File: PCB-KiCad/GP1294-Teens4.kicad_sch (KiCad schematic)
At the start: 13 parts, among them U8 CS8421

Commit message: Fixed merge issues.
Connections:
- net DATA_OUT: now also U8.5 (DATA_OUT)
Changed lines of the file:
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@@
+    (stroke (width 0) (type default))
+  )
+  (wire (pts (xy 129.54 51.308) (xy 113.284 51.308))
     (stroke (width 0) (type default))
   )

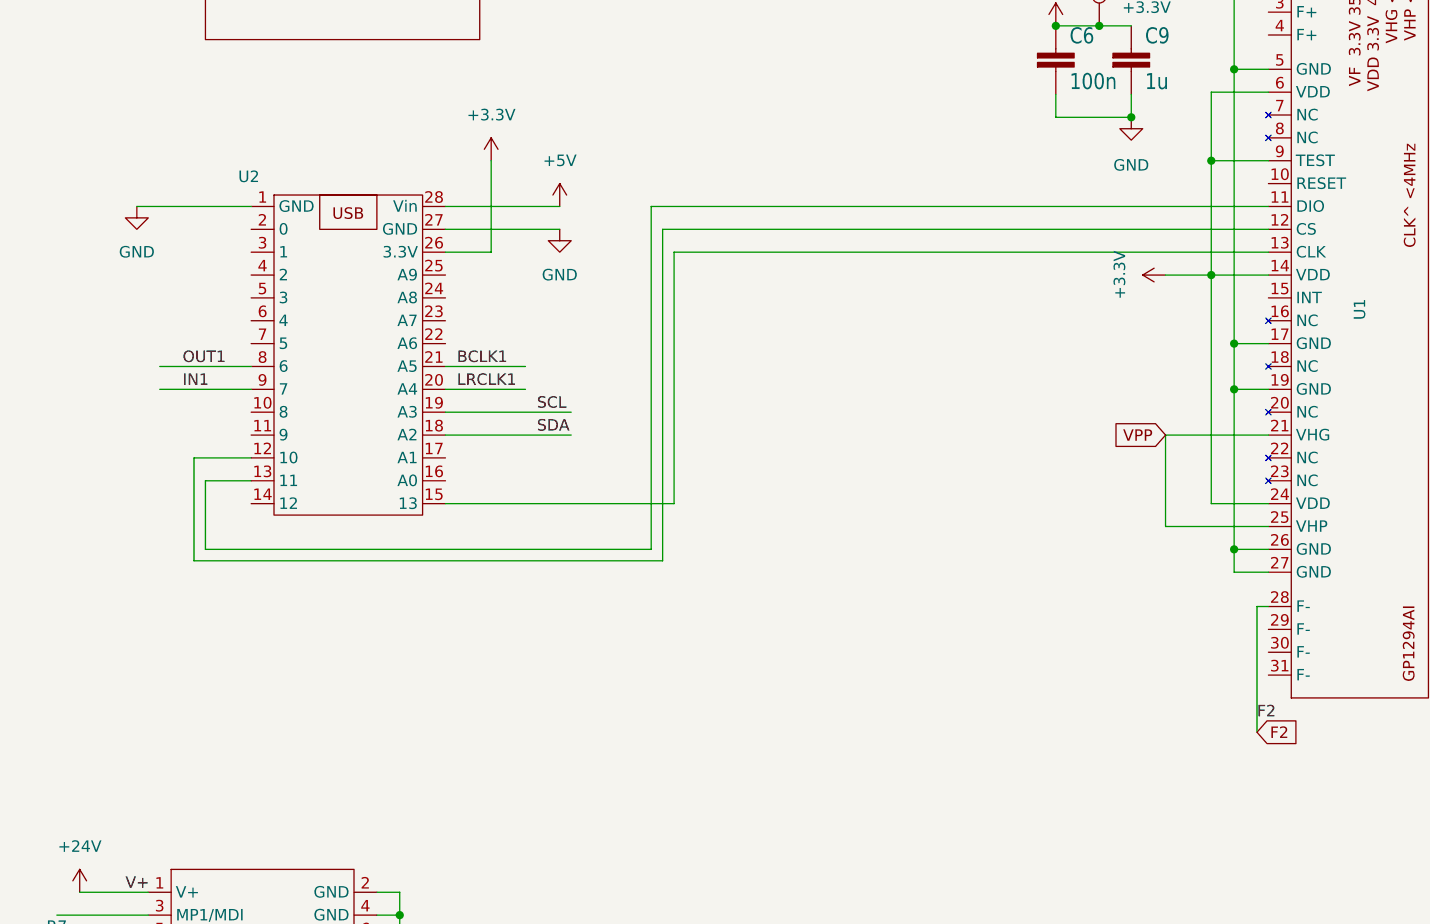
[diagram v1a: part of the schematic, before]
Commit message: Added OLED 5.5" option
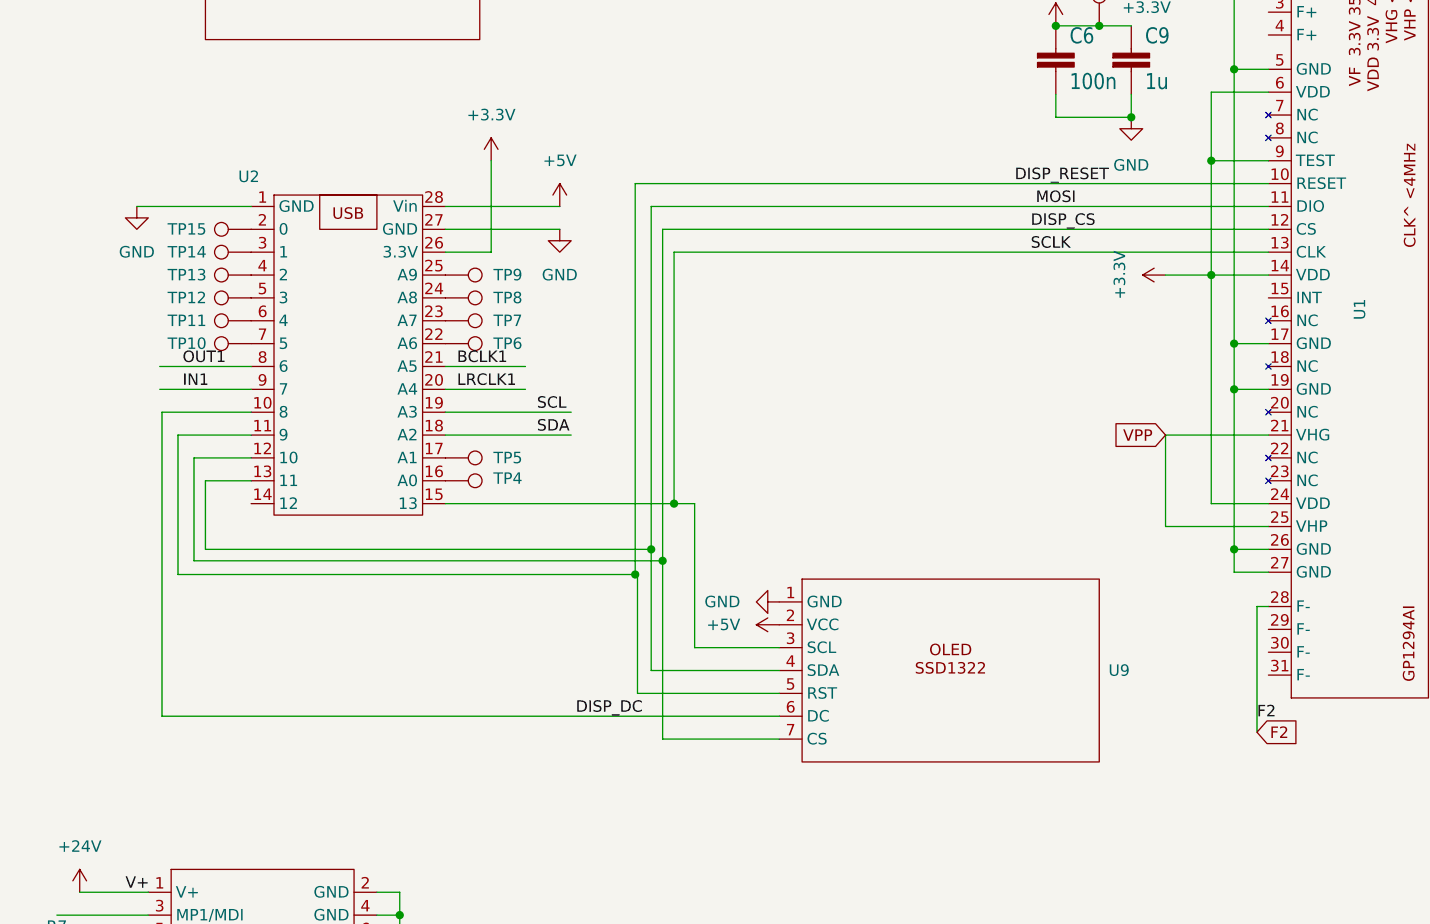
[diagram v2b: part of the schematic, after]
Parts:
- added TP10, TP11, TP12, TP13, TP14, TP15, TP4, TP5, TP6, TP7, TP8, TP9: TestPoint, TestPoint:TestPoint_Pad_2.0x2.0mm, symbol Connector:TestPoint
- added U9: ~, VFDs-Library:OLED5.5, symbol VFDs-Library:OLED5.5
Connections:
- net +5V: now also U9.2 (VCC)
- net GND: now also U9.1 (GND)
- net DISP_RESET: now reaches U1.10 (RESET)
- net DISP_RESET: now also U2.11 (9), U9.5 (RST)
- net MOSI: now reaches U1.11 (DIO), U2.13 (11)
- net MOSI: now also U9.4 (SDA)
- net DISP_CS: now reaches U1.12 (CS), U2.12 (10)
- net DISP_CS: now also U9.7 (CS)
- net SCLK: now reaches U1.13 (CLK), U2.15 (13)
- net SCLK: now also U9.3 (SCL)
- net DISP_DC: now reaches U2.10 (8)
- net DISP_DC: now also U9.6 (DC)
- net at U2.16 (A0): now also TP4.1
- net at U2.17 (A1): now also TP5.1
- net at U2.2 (0): now also TP15.1
- net at U2.22 (A6): now also TP6.1
- net at U2.23 (A7): now also TP7.1
- net at U2.24 (A8): now also TP8.1
- net at U2.25 (A9): now also TP9.1
- net at U2.3 (1): now also TP14.1
- net at U2.4 (2): now also TP13.1
- net at U2.5 (3): now also TP12.1
- net at U2.6 (4): now also TP11.1
- net at U2.7 (5): now also TP10.1

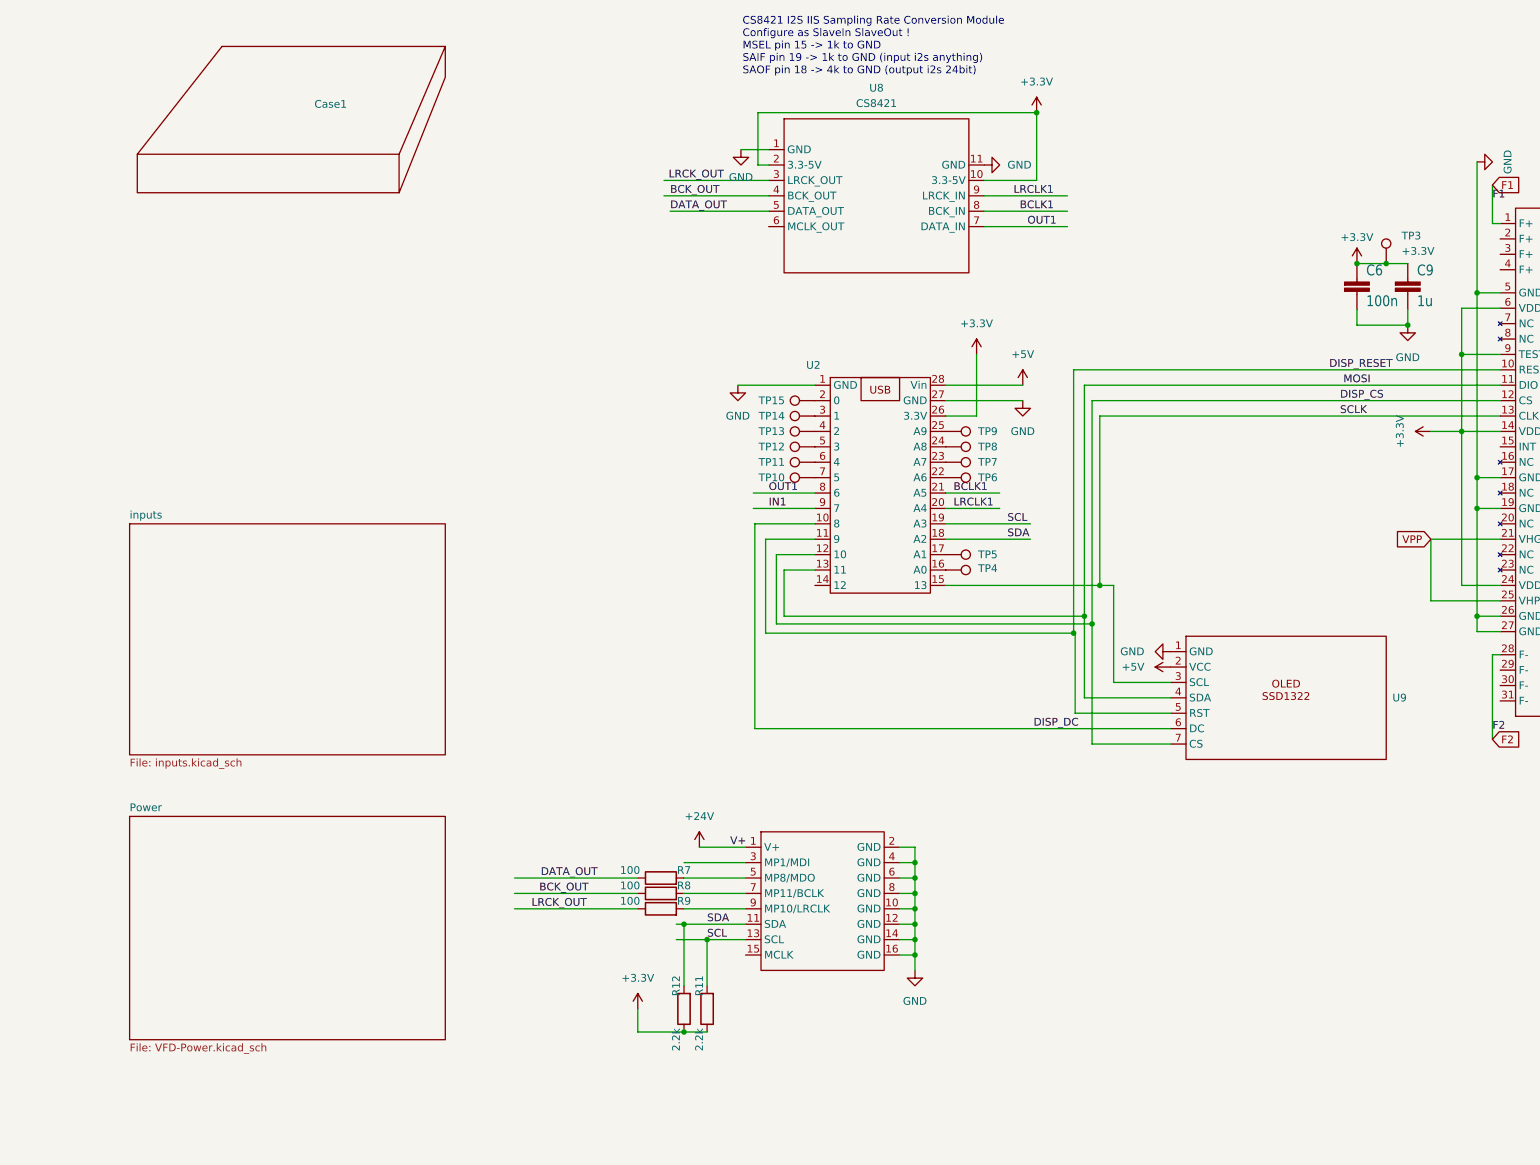
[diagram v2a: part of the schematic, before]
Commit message: Upgraded Power circuit.
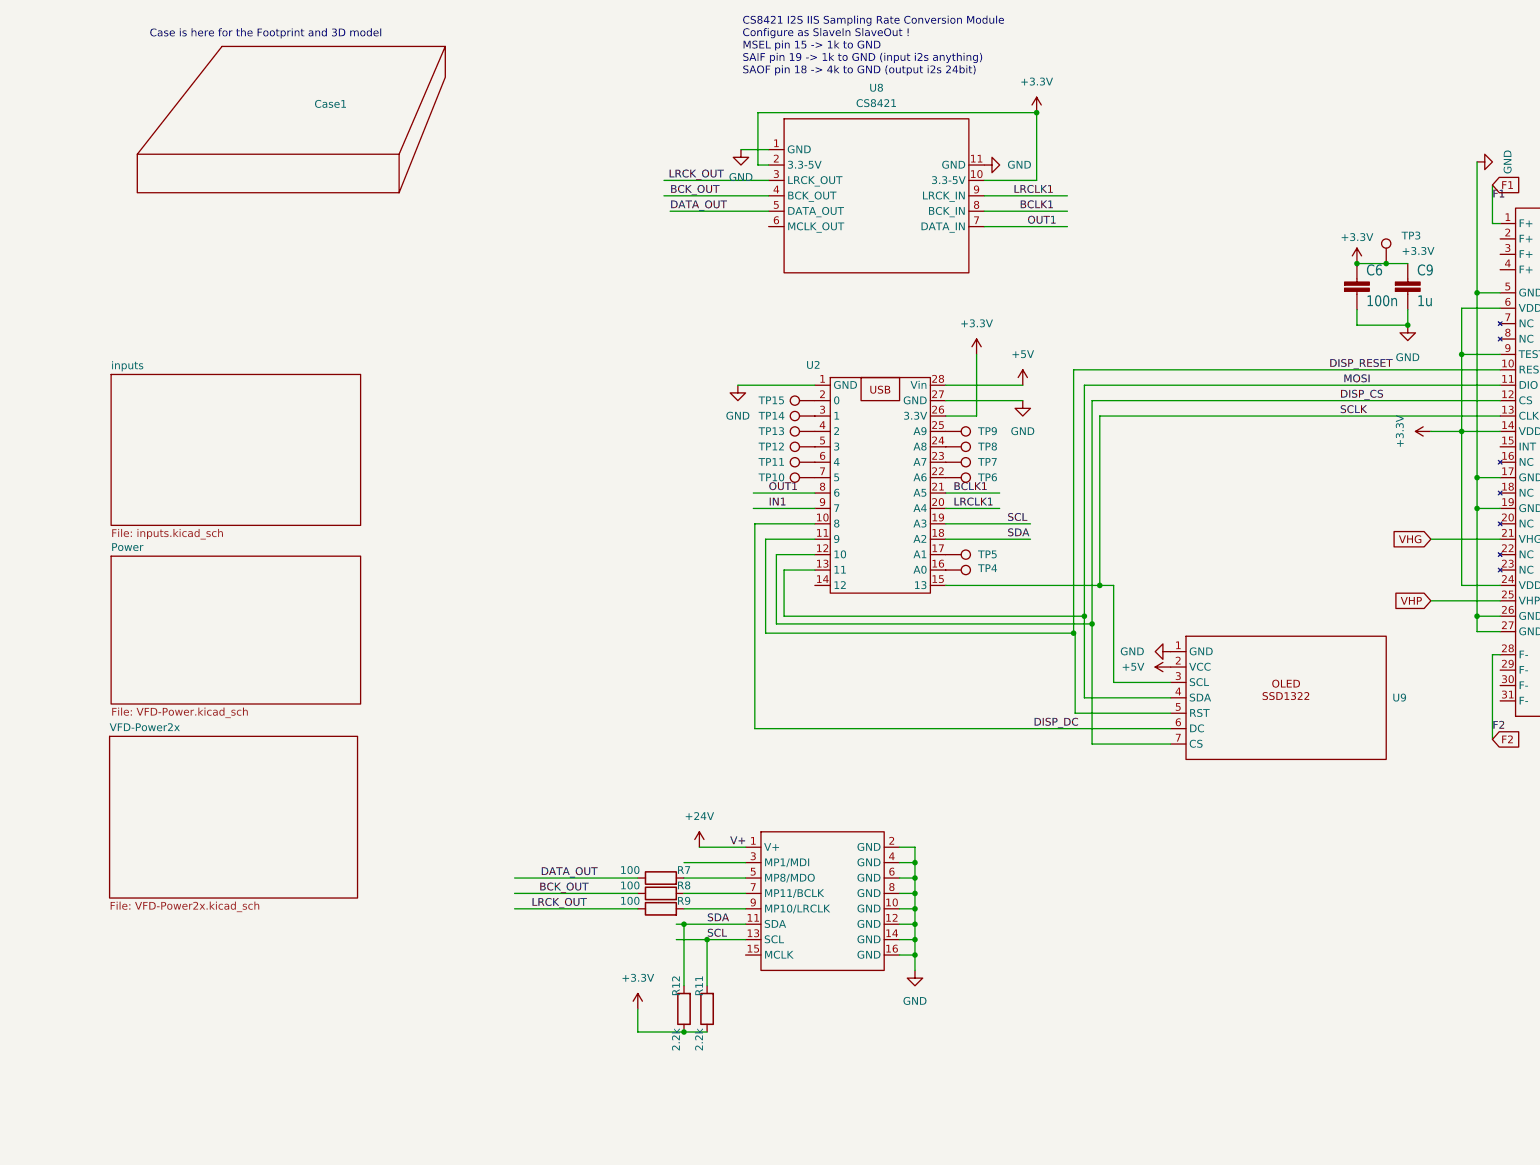
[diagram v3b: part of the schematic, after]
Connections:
- net VPP renamed VHG
- net VHG: no longer U1.25 (VHP)
- new net VHP: U1.25 (VHP)
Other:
- added sheet VFD-Power2x (VFD-Power2x.kicad_sch)
- note added: "Case is here for the Footprint and 3D model"
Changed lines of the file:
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@@
-    (stroke (width 0) (type default))
-  )
-  (wire (pts (xy 238.76 115.57) (xy 238.76 105.41))
     (stroke (width 0) (type default))
   )
@@
   (wire (pts (xy 124.968 41.148) (xy 129.54 41.148))
     (stroke (width 0) (type default))
+  )
+  (text "Case is here for the Footprint and 3D model" (at 27.432 22.86 0)
+    (effects (font (size 1.27 1.27)) (justify left bottom))
   )
   (text "CS8421 I2S IIS Sampling Rate Conversion Module\nConfigure as SlaveIn SlaveOut !\nMSEL pin 15 -> 1k to GND\nSAIF pin 19 -> 1k to GND (input i2s anything)\nSAOF pin 18 -> 4k to GND (output i2s 24bit)"
@@
     )
   )
-  (global_label "VPP" (shape input) (at 238.76 105.41 180) (fields_autoplaced)
+  (global_label "VHG" (shape input) (at 238.76 105.41 180) (fields_autoplaced)
     (effects (font (size 1.27 1.27)) (justify right))
-    (property "Intersheetrefs" "${INTERSHEET_REFS}" (at 232.1462 105.41 0)
+    (property "Intersheetrefs" "${INTERSHEET_REFS}" (at 232.0857 105.41 0)
+      (effects (font (size 1.27 1.27)) (justify right) hide)
+    )
+  )
+  (global_label "VHP" (shape input) (at 238.76 115.57 180) (fields_autoplaced)
+    (effects (font (size 1.27 1.27)) (justify right))
+    (property "Intersheetrefs" "${INTERSHEET_REFS}" (at 232.0857 115.57 0)
       (effects (font (size 1.27 1.27)) (justify right) hide)
     )
@@
     )
   )
-  (sheet (at 24.13 102.87) (size 52.07 38.1) (fields_autoplaced)
+  (sheet (at 21.082 78.232) (size 41.148 24.892) (fields_autoplaced)
     (stroke (width 0.1524) (type solid))
     (fill (color 0 0 0 0.0000))
-    (property "Sheetname" "inputs" (at 24.13 102.1584 0)
+    (property "Sheetname" "inputs" (at 21.082 77.5204 0)
       (effects (font (size 1.27 1.27)) (justify left bottom))
     )
-    (property "Sheetfile" "inputs.kicad_sch" (at 24.13 141.5546 0)
+    (property "Sheetfile" "inputs.kicad_sch" (at 21.082 103.7086 0)
       (effects (font (size 1.27 1.27)) (justify left top))
     )
@@
     )
   )
-  (sheet (at 24.13 151.13) (size 52.07 36.83) (fields_autoplaced)
+  (sheet (at 21.082 108.204) (size 41.148 24.384) (fields_autoplaced)
     (stroke (width 0.1524) (type solid))
     (fill (color 0 0 0 0.0000))
-    (property "Sheetname" "Power" (at 24.13 150.4184 0)
+    (property "Sheetname" "Power" (at 21.082 107.4924 0)
       (effects (font (size 1.27 1.27)) (justify left bottom))
     )
-    (property "Sheetfile" "VFD-Power.kicad_sch" (at 24.13 188.5446 0)
+    (property "Sheetfile" "VFD-Power.kicad_sch" (at 21.082 133.1726 0)
       (effects (font (size 1.27 1.27)) (justify left top))
     )
@@
       )
     )
+  )
+  (sheet (at 20.828 137.922) (size 40.894 26.67) (fields_autoplaced)
+    (stroke (width 0.1524) (type solid))
+    (fill (color 0 0 0 0.0000))
+    (property "Sheetname" "VFD-Power2x" (at 20.828 137.2104 0)
+      (effects (font (size 1.27 1.27)) (justify left bottom))
+    )
+    (property "Sheetfile" "VFD-Power2x.kicad_sch" (at 20.828 165.1766 0)
+      (effects (font (size 1.27 1.27)) (justify left top))
+    )
+    (instances
+      (project "GP1294-Teens4"
+        (path "/3de011e3-f89b-42a8-8637-1f4c3f0867fa" (page "4"))
+      )
+    )
